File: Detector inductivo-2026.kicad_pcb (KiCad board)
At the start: 2 copper layers, 199 x 37 mm, 84 parts, among them Q1 2N2222A, Q10 BC557, Q11 BC557, Q12 2N2222A, Q13 2N2222A, Q14 BC557, Q15 BC557, Q16 2N2222A, Q2 BC557, Q3 BC557, Q4 2N2222A, Q5 2N2222A, Q6 BC557, Q7 BC557, Q8 2N2222A, Q9 2N2222A

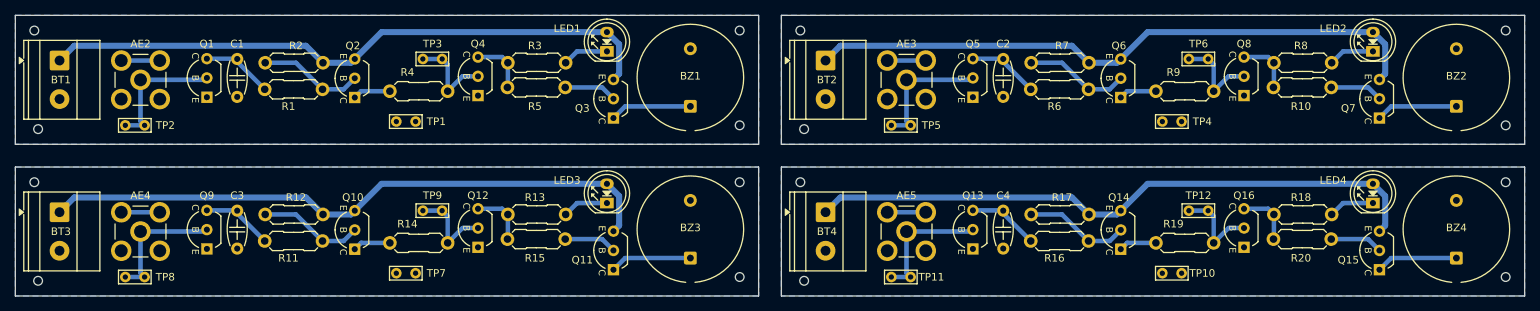
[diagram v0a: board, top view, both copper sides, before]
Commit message: Se agregaron lágrimas a los pads
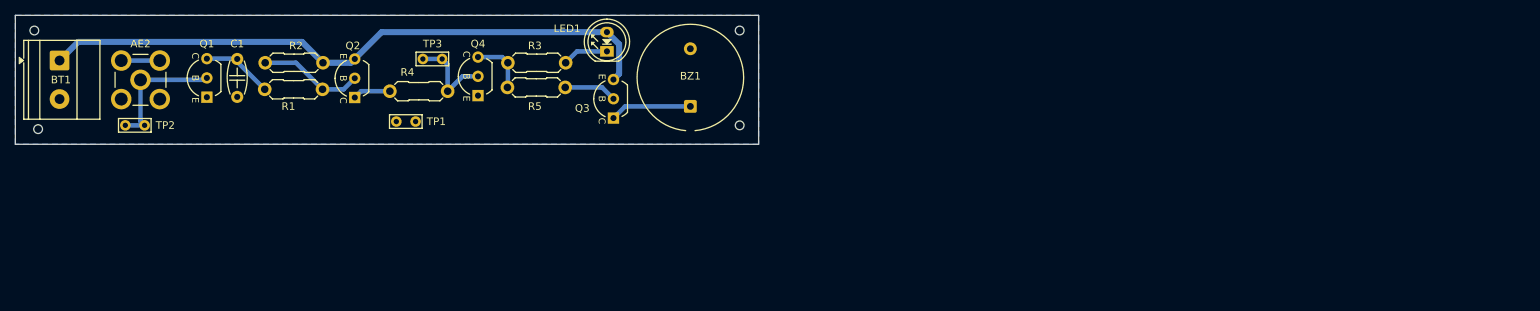
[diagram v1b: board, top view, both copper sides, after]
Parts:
- removed AE3, AE4, AE5: Antenna_Shield, Conector_sma:SMA_Amphenol_132134-11_Vertical
- removed BT2, BT3, BT4: Battery, TerminalBlock_Phoenix:TerminalBlock_Phoenix_MKDS-1,5-2-5.08_1x02_P5.08mm_Horizontal
- removed BZ2, BZ3, BZ4: Buzzer, Buzzer_Beeper:Indicator_PUI_AI-1440-TWT-24V-2-R
- removed C2, C3, C4: 100nF, PCM_Capacitor_THT_AKL:C_Disc_D4.7mm_W2.5mm_P5.00mm
- removed H10, H11, H12, H13, H14, H15, H16, H5, H6, H7, H8, H9: MountingHole, MountingHole:ToolingHole_1.152mm
- removed LED2, LED3, LED4: LED_5mm_Green, PCM_LED_THT_AKL:LED_D5.0mm
- removed Q10, Q11, Q14, Q15, Q6, Q7: BC557, PCM_Package_TO_SOT_THT_AKL:TO-92_Inline_Wide_CBE
- removed Q12, Q13, Q16, Q5, Q8, Q9: 2N2222A, PCM_Package_TO_SOT_THT_AKL:TO-92_Inline_Wide_EBC
- removed R10, R15, R20: 10k, Resistencias:R_Axial_DIN0207_L6.3mm_D2.5mm_P7.62mm_Horizontal
- removed R11, R14, R16, R19, R6, R9: 100k, Resistencias:R_Axial_DIN0207_L6.3mm_D2.5mm_P7.62mm_Horizontal
- removed R12, R17, R7: 1M, Resistencias:R_Axial_DIN0207_L6.3mm_D2.5mm_P7.62mm_Horizontal
- removed R13, R18, R8: 47, Resistencias:R_Axial_DIN0207_L6.3mm_D2.5mm_P7.62mm_Horizontal
- removed TP10, TP11, TP12, TP4, TP5, TP6, TP7, TP8, TP9: TestPoint_Probe, TestPoint:TestPoint_Bridge_Pitch2.54mm_Drill0.7mm
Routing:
- net /9V: track 331.2 -> 83.2 mm
- net Net-(AE2-A): track 70.5 -> 17.6 mm
- net Net-(Q2-B): track 55.5 -> 13.9 mm
- net Net-(Q4-B): track 47.6 -> 11.9 mm
- net Net-(BZ1-+): track 43.1 -> 10.8 mm
- net Net-(Q1-C): track 38.1 -> 9.52 mm
- net Net-(Q4-C): track 30.1 -> 7.53 mm
- net Net-(Q3-B): track 27.9 -> 6.98 mm
- net Net-(LED1-K): track 24.2 -> 6.06 mm
- net GND: track 20.3 -> 5.08 mm
- net Net-(Q2-C): track 19.9 -> 4.97 mm
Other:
- board size 199 x 37 mm -> 98 x 17 mm
